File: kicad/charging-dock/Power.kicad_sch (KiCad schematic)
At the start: 29 parts, among them U1 XT220UF50V90RV0078, U2 1206L300SL16ARG, U22 AP64501SP-13, U6 BV1HAL45EFJ-E2

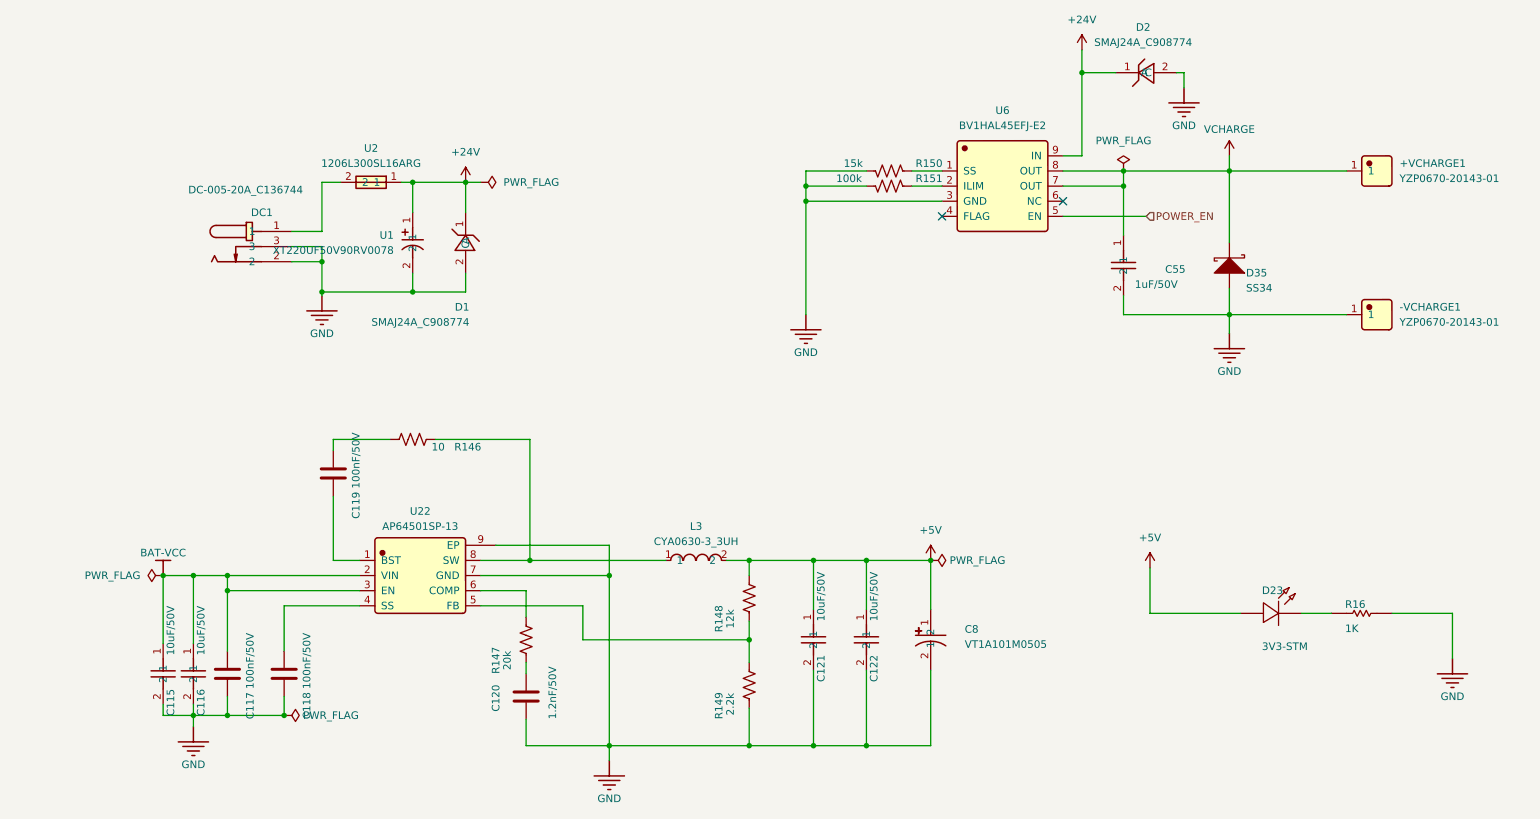
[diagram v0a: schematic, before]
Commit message: Charging dock rev 2; main-phone bucks AP64501 -> TPS54560B
Charging dock (kicad/charging-dock), redesigned:
- CH32V003F4P6 control (Arduino core, ch32fun, PlatformIO)
- robot detection: resistance-signature probe before DOCK+ goes live
- AO4407C soft-start output switch, 50 mOhm + INA180A1 current sense
- NEC IR beacon: two 3x TSAL6200 strings, AC-coupled gates
- 20 V input: DC-044A-20A, 5 A fuse, SMAJ22A, HT7533-1
- refs 8xxx for the one-panel plan; uses the shared ../main libraries
- removed the orphan sheets, the old local library copy and an unrelated PDF
- README with pin map, detection math, firmware rules, layout notes

main-phone: U21/U22 TPS54560B (AP64501 out of stock) with SS56 catch
diodes, 232k RT, 4.7k + 47nF compensation, U21 EN divider; BAT-VCC input
caps 10uF/50V 1206. SPEC and READMEs updated.

Co-Authored-By: Claude Opus 5.5 (1M context) <noreply@anthropic.com>
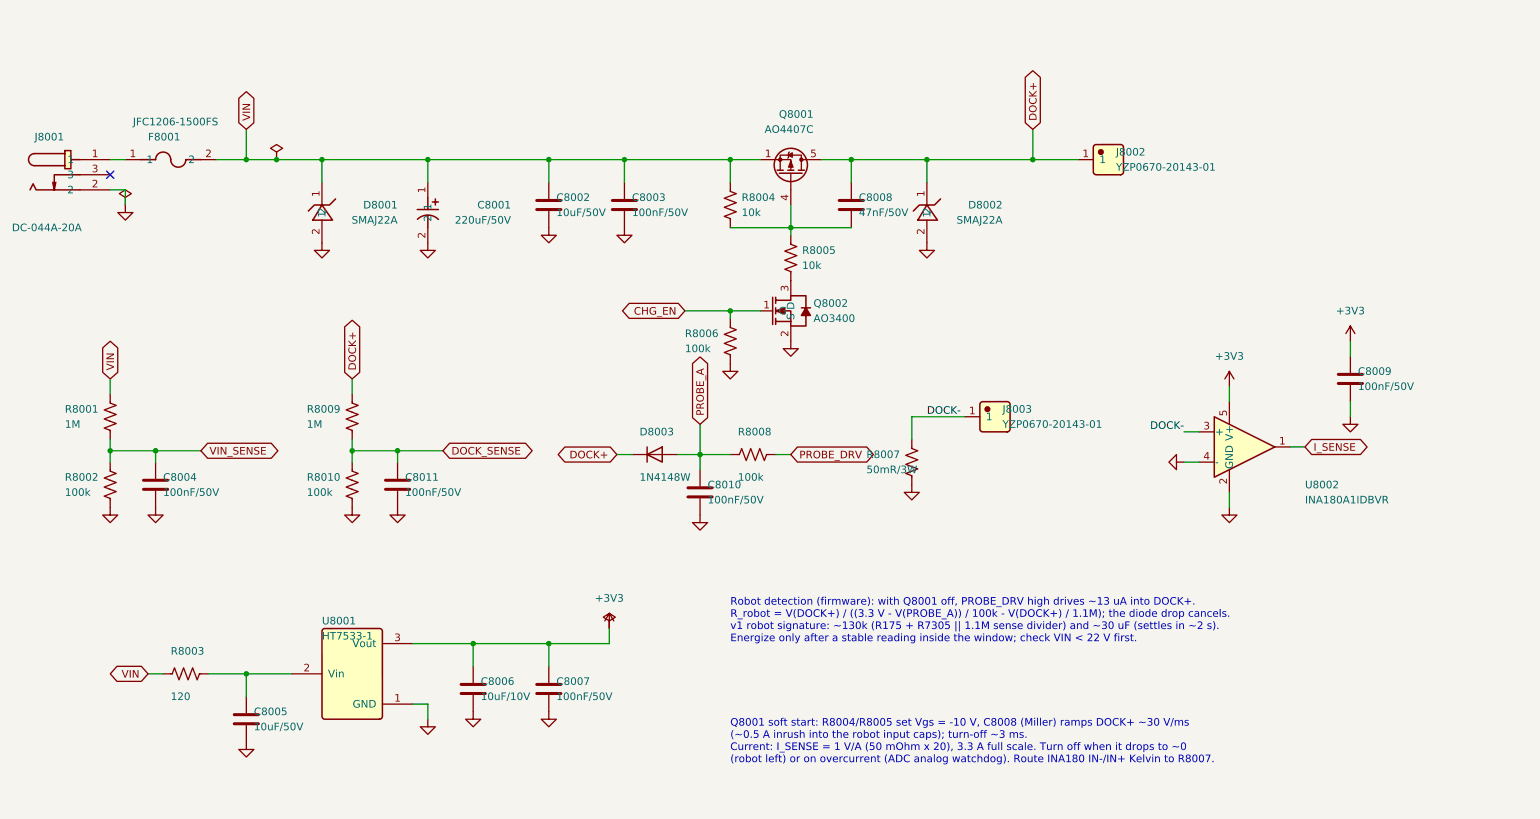
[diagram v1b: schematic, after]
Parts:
- removed +VCHARGE1, -VCHARGE1: YZP0670-20143-01, JLCImport:YZP0670-20143-01, symbol JLCImport:YZP0670-20143-01
- removed C115, C116, C121, C122: 10uF/50V, Capacitor_SMD:C_0603_1608Metric, symbol JLCImport:CL21A106KBYQNNE
- removed C117, C118, C119: 100nF/50V, Capacitor_SMD:C_0603_1608Metric, symbol Library:C_0603
- removed C120: 1.2nF/50V, Capacitor_SMD:C_0603_1608Metric, symbol Library:C_0603
- removed C55: 1uF/50V, Capacitor_SMD:C_0603_1608Metric, symbol JLCImport:CL21A106KBYQNNE
- removed C8: VT1A101M0505, JLCImport:VT1A101M0505, symbol JLCImport:VT1A101M0505
- removed D1, D2: SMAJ24A_C908774, JLCImport:SMAJ24A_C908774, symbol JLCImport:SMAJ24A_C908774
- removed D23: 3V3-STM, oomwoo_altium:LED0603-B, symbol DesignLibrary:POWER_0_LED-SMD_DesignLibrary.SchLib
- removed D35: SS34, oomwoo_altium:SMA, symbol DesignLibrary:MAIN-BRUSH MOTOR_1_DIODE-2_DesignLibrary.SchLib
- removed DC1: DC-005-20A_C136744, JLCImport:DC-005-20A_C136744, symbol JLCImport:DC-005-20A_C136744
- removed L3: CYA0630-3_3UH, JLCImport:CYA0630-3_3UH, symbol JLCImport:CYA0630-3_3UH
- removed R146: 10, symbol Device:R_US
- removed R147: 20k, symbol Device:R_US
- removed R148: 12k, symbol Device:R_US
- removed R149: 2.2k, symbol Device:R_US
- removed R150: 15k, symbol Device:R_US
- removed R151: 100k, symbol Device:R_US
- removed R16: 1K, Resistor_SMD:R_0603_1608Metric, symbol DesignLibrary:POWER_2_Resistor-1_DesignLibrary.SchLib
- removed U1: XT220UF50V90RV0078, JLCImport:XT220UF50V90RV0078, symbol JLCImport:XT220UF50V90RV0078
- removed U2: 1206L300SL16ARG, JLCImport:1206L300SL16ARG, symbol JLCImport:1206L300SL16ARG
- removed U22: AP64501SP-13, JLCImport:AP64501SP-13, symbol JLCImport:AP64501SP-13
- removed U6: BV1HAL45EFJ-E2, JLCImport:BV1HAL45EFJ-E2, symbol JLCImport:BV1HAL45EFJ-E2
- added C8001: 220uF/50V, JLCImport:XT220UF50V90RV0078, symbol JLCImport:XT220UF50V90RV0078
- added C8002, C8005: 10uF/50V, Capacitor_SMD:C_1206_3216Metric, symbol Device:C
- added C8003, C8004, C8007, C8009, C8010, C8011: 100nF/50V, Capacitor_SMD:C_0603_1608Metric, symbol Device:C
- added C8006: 10uF/10V, Capacitor_SMD:C_0603_1608Metric, symbol Device:C
- added C8008: 47nF/50V, Capacitor_SMD:C_0603_1608Metric, symbol Device:C
- added D8001, D8002: SMAJ22A, JLCImport:SMAJ18A_C148219, symbol JLCImport:SMAJ18A_C148219
- added D8003: 1N4148W, Diode_SMD:D_SOD-123, symbol Device:D
- added F8001: JFC1206-1500FS, JLCImport:JFC1206-2200FS, symbol JLCImport:JFC1206-2200FS
- added J8001: DC-044A-20A, JLCImport:DC-044A-20A, symbol JLCImport:DC-005-5A-2_0
- added J8002, J8003: YZP0670-20143-01, JLCImport:YZP0670-20143-01, symbol JLCImport:YZP0670-20143-01
- added Q8001: AO4407C, Package_SO:SOIC-8_3.9x4.9mm_P1.27mm, symbol JLCImport:AO4407C
- added Q8002: AO3400, JLCImport:AO3400, symbol JLCImport:AO3400
- added R8001, R8009: 1M, Resistor_SMD:R_0603_1608Metric, symbol Device:R_US
- added R8002, R8006, R8008, R8010: 100k, Resistor_SMD:R_0603_1608Metric, symbol Device:R_US
- added R8003: 120, Resistor_SMD:R_0603_1608Metric, symbol Device:R_US
- added R8004, R8005: 10k, Resistor_SMD:R_0603_1608Metric, symbol Device:R_US
- added R8007: 50mR/3W, Resistor_SMD:R_2512_6332Metric, symbol Device:R_US
- added U8001: HT7533-1, JLCImport:HT7533-1_C14289, symbol JLCImport:HT7533-1_C14289
- added U8002: INA180A1IDBVR, Package_TO_SOT_SMD:SOT-23-5, symbol Amplifier_Current:INA180A1
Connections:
- net GND: now also C8001.2, C8002.2, C8003.2, C8004.2, C8005.2, C8006.2, C8007.2, C8009.2, C8010.2, C8011.2, D8001.2, D8002.2, J8001.2, Q8002.2 (S), R8002.2, R8006.2, R8007.2, R8010.2, U8001.1 (GND), U8002.2 (GND), U8002.4 (-)
- new net: C8008.2, Q8001.4 (G), R8004.2, R8005.1
- new net: F8001.1, J8001.1
- new net: C8005.1, R8003.2, U8001.2 (Vin)
- new net: Q8002.3 (D), R8005.2
- new net +3V3: C8006.1, C8007.1, C8009.1, U8001.3 (Vout), U8002.5 (V+)
- new net CHG_EN: Q8002.1 (G), R8006.1
- new net DOCK+: C8008.1, D8002.1, D8003.1 (K), J8002.1, Q8001.5 (D), Q8001.6 (D), Q8001.7 (D), Q8001.8 (D), R8009.1
- new net DOCK-: J8003.1, R8007.1, U8002.3 (+)
- new net DOCK_SENSE: C8011.1, R8009.2, R8010.1
- new net I_SENSE: U8002.1
- new net PROBE_A: C8010.1, D8003.2 (A), R8008.1
- new net PROBE_DRV: R8008.2
- new net VIN: C8001.1, C8002.1, C8003.1, D8001.1, F8001.2, Q8001.1 (S), Q8001.2 (S), Q8001.3 (S), R8001.1, R8003.1, R8004.1
- new net VIN_SENSE: C8004.1, R8001.2, R8002.1
- no-connect marks 2 -> 1
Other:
- note added: "Q8001 soft start: R8004/R8005 set Vgs = -10 V, C8008 (Miller) ramps DOCK+ ~30 V/ms (~0.5 A inrush into the robot input caps); turn-off ~3 ms. Current: I_SENSE = 1 V/A (50 mOhm x 20), 3.3 A full scale. Turn off when it drops to ~0 (robot left) or on overcurrent (ADC analog watchdog). Route INA180 IN-/IN+ Kelvin to R8007."
- note added: "Robot detection (firmware): with Q8001 off, PROBE_DRV high drives ~13 uA into DOCK+. R_robot = V(DOCK+) / ((3.3 V - V(PROBE_A)) / 100k - V(DOCK+) / 1.1M); the diode drop cancels. v1 robot signature: ~130k (R175 + R7305 || 1.1M sense divider) and ~30 uF (settles in ~2 s). Energize only after a stable reading inside the window; check VIN < 22 V first."
- company: (none) -> OOMWOO charging dock
- title: (none) -> Power

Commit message: Per-board reference ranges, J1 spare header, IMU AD0 pull-down, BOM outputs
- reference ranges: main-phone 1-999, dock 1000s, front ToF 2000s, side 3000s,
  cliff 4000s, rear IR 5000s, Hall 6000s (main-phone 7xxx parts renumbered
  below 1000; sensor boards and dock moved from 8xxx)
- main-phone: J7301 -> J1, a fitted 2x7 0.1" header with spares only
  (3.3 V, 5 V, I2C4, UART PC10/PC11, PA8-PA10, PD4, PE2, PE6, GND)
- IMU: AP_AD0 pulled low by R217 (address 0x68); INT2 on test pad TP1;
  FSYNC reachable on R211; R18/R72 removed
- tools/export.py replaces export_pdfs.py: schematic PDF and JLC-style BOM in
  each board's output/ folder; --pcb adds Gerbers, placement and STEP
- cliff and rear IR projects: fix top-level sheet left over from a copy
- Hall board: visual tidy-up

Co-Authored-By: Claude Opus 5.5 <noreply@anthropic.com>
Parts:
- renumbered C8001 to C1001, C8002 to C1002, C8003 to C1003, C8004 to C1004, C8005 to C1005, C8006 to C1006, C8007 to C1007, C8008 to C1008, C8009 to C1009, C8010 to C1010, C8011 to C1011, D8001 to D1001, D8002 to D1002, D8003 to D1003, F8001 to F1001, J8001 to J1001, J8002 to J1002, J8003 to J1003, Q8001 to Q1001, Q8002 to Q1002, R8001 to R1001, R8002 to R1002, R8003 to R1003, R8004 to R1004, R8005 to R1005, R8006 to R1006, R8007 to R1007, R8008 to R1008, R8009 to R1009, R8010 to R1010, U8001 to U1001, U8002 to U1002
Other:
- note added: "Q1001 soft start: R1004/R1005 set Vgs = -10 V, C1008 (Miller) ramps DOCK+ ~30 V/ms (~0.5 A inrush into the robot input caps); turn-off ~3 ms. Current: I_SENSE = 1 V/A (50 mOhm x 20), 3.3 A full scale. Turn off when it drops to ~0 (robot left) or on overcurrent (ADC analog watchdog). Route INA180 IN-/IN+ Kelvin to R1007."
- note added: "Robot detection (firmware): with Q1001 off, PROBE_DRV high drives ~13 uA into DOCK+. R_robot = V(DOCK+) / ((3.3 V - V(PROBE_A)) / 100k - V(DOCK+) / 1.1M); the diode drop cancels. v1 robot signature: ~130k (R175 + R7305 || 1.1M sense divider) and ~30 uF (settles in ~2 s). Energize only after a stable reading inside the window; check VIN < 22 V first."
- note removed: "Q8001 soft start: R8004/R8005 set Vgs = -10 V, C8008 (Miller) ramps DOCK+ ~30 V/ms (~0.5 A inrush into the robot input caps); turn-off ~3 ms. Current: I_SENSE = 1 V/A (50 mOhm x 20), 3.3 A full scale. Turn off when it drops to ~0 (robot left) or on overcurrent (ADC analog watchdog). Route INA180 IN-/IN+ Kelvin to R8007."
- note removed: "Robot detection (firmware): with Q8001 off, PROBE_DRV high drives ~13 uA into DOCK+. R_robot = V(DOCK+) / ((3.3 V - V(PROBE_A)) / 100k - V(DOCK+) / 1.1M); the diode drop cancels. v1 robot signature: ~130k (R175 + R7305 || 1.1M sense divider) and ~30 uF (settles in ~2 s). Energize only after a stable reading inside the window; check VIN < 22 V first."
